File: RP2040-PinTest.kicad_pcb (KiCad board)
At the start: 2 copper layers, 57.2 x 53.3 mm, 3 parts

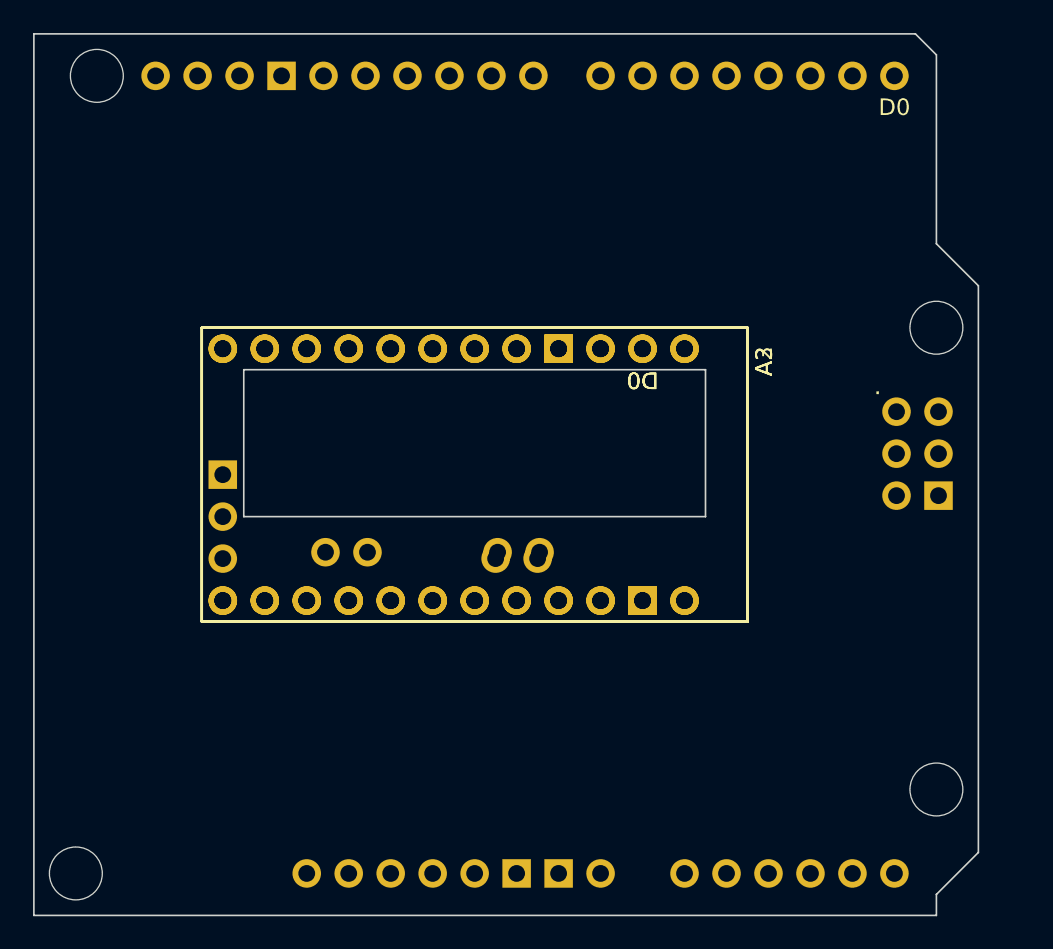
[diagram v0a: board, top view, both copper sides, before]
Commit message: Added more pins
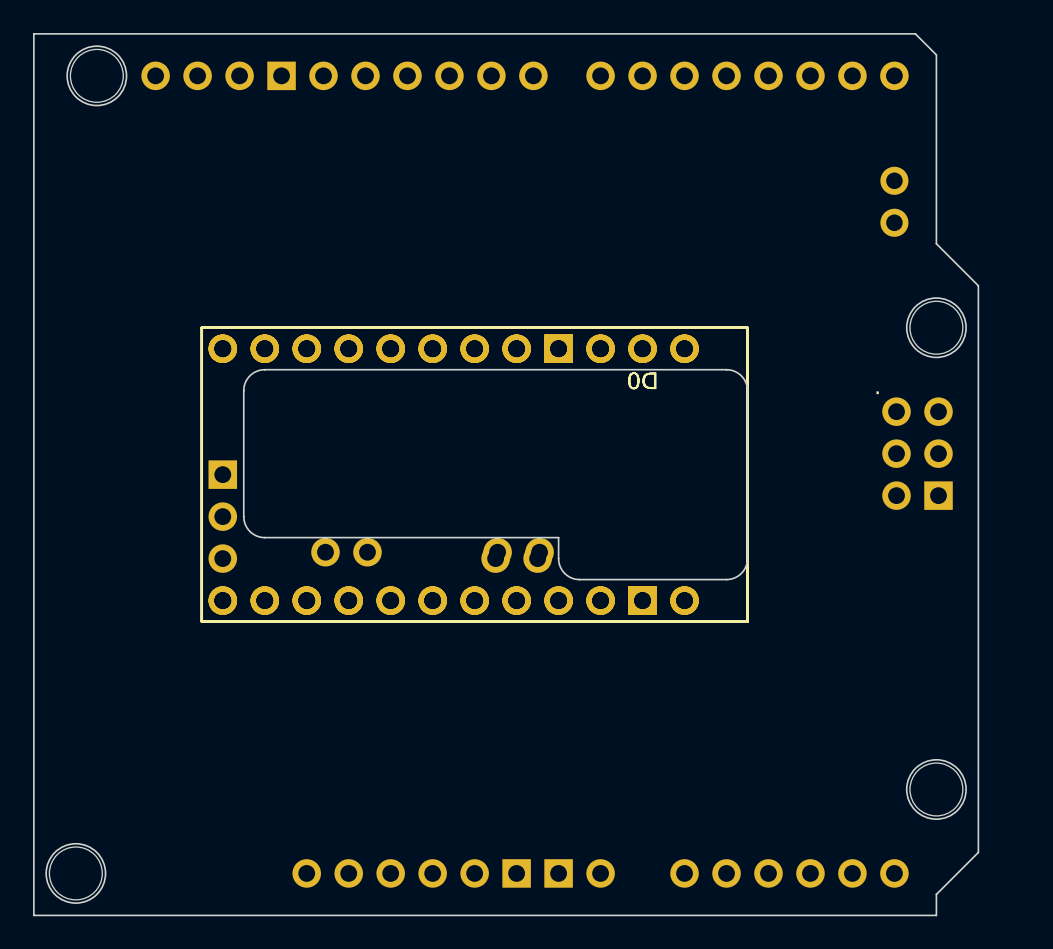
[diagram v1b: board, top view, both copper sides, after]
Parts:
- added J1: Conn_01x02_Socket, Connector_PinSocket_2.54mm:PinSocket_1x02_P2.54mm_Vertical, B.Cu at (182.9, 81.3)
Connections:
- A2 pad GND1: unconnected-(A2-GND-PadGND1) -> GND
- A2 pad GND2: unconnected-(A2-GND-PadGND2) -> GND
- A2 pad GND3: unconnected-(A2-GND-PadGND3) -> GND
- A3 pad GND1: unconnected-(A3-GND-PadGND1) -> GND
- A3 pad GND2: unconnected-(A3-GND-PadGND2) -> GND
- A4 pad GND1: unconnected-(A4-GND-PadGND1) -> GND
- A4 pad GND2: unconnected-(A4-GND-PadGND2) -> GND
- A4 pad GND3: unconnected-(A4-GND-PadGND3) -> GND
- A4 pad GND4: unconnected-(A4-SPI_GND-PadGND4) -> GND
- A4 pad MISO: unconnected-(A4-SPI_MISO-PadMISO) -> MISO
- A4 pad MOSI: unconnected-(A4-SPI_MOSI-PadMOSI) -> MOSI
- A4 pad SCK: unconnected-(A4-SPI_SCK-PadSCK) -> CSK
- A4 pad SCL: unconnected-(A4-PadSCL) -> SCL
- A4 pad SDA: unconnected-(A4-PadSDA) -> SDA
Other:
- outline, holes or cut-outs redrawn

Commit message: Added LEDs and basic routing
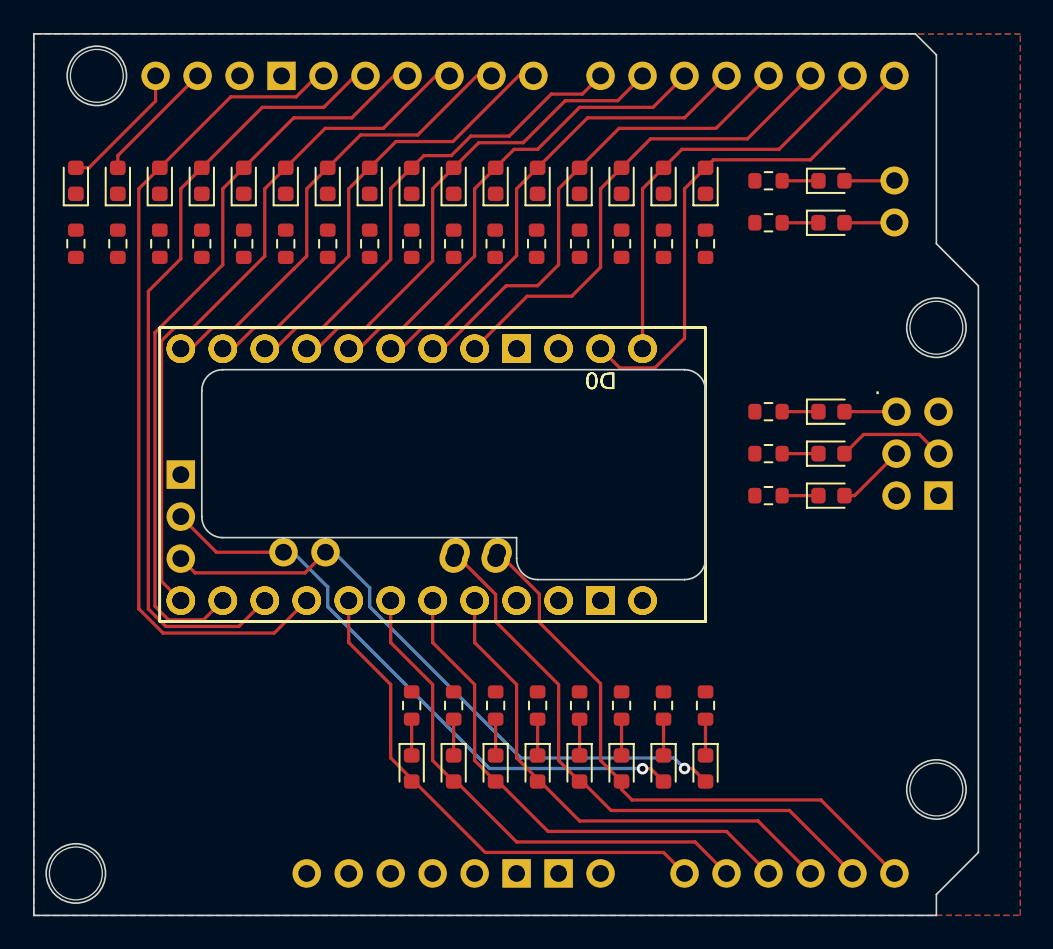
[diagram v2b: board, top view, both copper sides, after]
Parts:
- added D1: YELLOW, LED_SMD:LED_0603_1608Metric, F.Cu at (171.4, 81.3)
- added D10: YELLOW, LED_SMD:LED_0603_1608Metric, F.Cu at (148.6, 81.3)
- added D11: YELLOW, LED_SMD:LED_0603_1608Metric, F.Cu at (146.1, 81.3)
- added D12: YELLOW, LED_SMD:LED_0603_1608Metric, F.Cu at (143.5, 81.3)
- added D13: YELLOW, LED_SMD:LED_0603_1608Metric, F.Cu at (141.0, 81.3)
- added D14: YELLOW, LED_SMD:LED_0603_1608Metric, F.Cu at (138.4, 81.3)
- added D15: YELLOW, LED_SMD:LED_0603_1608Metric, F.Cu at (133.3, 81.3)
- added D16: YELLOW, LED_SMD:LED_0603_1608Metric, F.Cu at (135.9, 81.3)
- added D17: YELLOW, LED_SMD:LED_0603_1608Metric, F.Cu at (179.1, 95.2)
- added D18: YELLOW, LED_SMD:LED_0603_1608Metric, F.Cu at (179.1, 97.8)
- added D19: YELLOW, LED_SMD:LED_0603_1608Metric, F.Cu at (179.1, 100.3)
- added D2: YELLOW, LED_SMD:LED_0603_1608Metric, F.Cu at (168.9, 81.3)
- added D20: YELLOW, LED_SMD:LED_0603_1608Metric, F.Cu at (153.7, 116.8)
- added D21: YELLOW, LED_SMD:LED_0603_1608Metric, F.Cu at (156.2, 116.8)
- added D22: YELLOW, LED_SMD:LED_0603_1608Metric, F.Cu at (158.8, 116.8)
- added D23: YELLOW, LED_SMD:LED_0603_1608Metric, F.Cu at (161.3, 116.8)
- added D24: YELLOW, LED_SMD:LED_0603_1608Metric, F.Cu at (163.8, 116.8)
- added D25: YELLOW, LED_SMD:LED_0603_1608Metric, F.Cu at (166.4, 116.8)
- added D26: YELLOW, LED_SMD:LED_0603_1608Metric, F.Cu at (168.9, 116.8)
- added D27: YELLOW, LED_SMD:LED_0603_1608Metric, F.Cu at (171.4, 116.8)
- added D28: YELLOW, LED_SMD:LED_0603_1608Metric, F.Cu at (179.1, 83.8)
- added D29: YELLOW, LED_SMD:LED_0603_1608Metric, F.Cu at (179.1, 81.3)
- added D3: YELLOW, LED_SMD:LED_0603_1608Metric, F.Cu at (166.4, 81.3)
- added D4: YELLOW, LED_SMD:LED_0603_1608Metric, F.Cu at (163.8, 81.3)
- added D5: YELLOW, LED_SMD:LED_0603_1608Metric, F.Cu at (161.3, 81.3)
- added D6: YELLOW, LED_SMD:LED_0603_1608Metric, F.Cu at (158.8, 81.3)
- added D7: YELLOW, LED_SMD:LED_0603_1608Metric, F.Cu at (156.2, 81.3)
- added D8: YELLOW, LED_SMD:LED_0603_1608Metric, F.Cu at (153.7, 81.3)
- added D9: YELLOW, LED_SMD:LED_0603_1608Metric, F.Cu at (151.1, 81.3)
- added R1: 5k1, Resistor_SMD:R_0603_1608Metric, F.Cu at (171.4, 85.1)
- added R10: 5k1, Resistor_SMD:R_0603_1608Metric, F.Cu at (148.6, 85.1)
- added R11: 5k1, Resistor_SMD:R_0603_1608Metric, F.Cu at (146.1, 85.1)
- added R12: 5k1, Resistor_SMD:R_0603_1608Metric, F.Cu at (143.5, 85.1)
- added R13: 5k1, Resistor_SMD:R_0603_1608Metric, F.Cu at (141.0, 85.1)
- added R14: 5k1, Resistor_SMD:R_0603_1608Metric, F.Cu at (138.4, 85.1)
- added R15: 5k1, Resistor_SMD:R_0603_1608Metric, F.Cu at (133.3, 85.1)
- added R16: 5k1, Resistor_SMD:R_0603_1608Metric, F.Cu at (135.9, 85.1)
- added R17: 5k1, Resistor_SMD:R_0603_1608Metric, F.Cu at (175.3, 95.2)
- added R18: 5k1, Resistor_SMD:R_0603_1608Metric, F.Cu at (175.3, 97.8)
- added R19: 5k1, Resistor_SMD:R_0603_1608Metric, F.Cu at (175.3, 100.3)
- added R2: 5k1, Resistor_SMD:R_0603_1608Metric, F.Cu at (168.9, 85.1)
- added R20: 5k1, Resistor_SMD:R_0603_1608Metric, F.Cu at (153.7, 113.0)
- added R21: 5k1, Resistor_SMD:R_0603_1608Metric, F.Cu at (156.2, 113.0)
- added R22: 5k1, Resistor_SMD:R_0603_1608Metric, F.Cu at (158.8, 113.0)
- added R23: 5k1, Resistor_SMD:R_0603_1608Metric, F.Cu at (161.3, 113.0)
- added R24: 5k1, Resistor_SMD:R_0603_1608Metric, F.Cu at (163.8, 113.0)
- added R25: 5k1, Resistor_SMD:R_0603_1608Metric, F.Cu at (166.4, 113.0)
- added R26: 5k1, Resistor_SMD:R_0603_1608Metric, F.Cu at (168.9, 113.0)
- added R27: 5k1, Resistor_SMD:R_0603_1608Metric, F.Cu at (171.4, 113.0)
- added R28: 5k1, Resistor_SMD:R_0603_1608Metric, F.Cu at (175.3, 83.8)
- added R29: 5k1, Resistor_SMD:R_0603_1608Metric, F.Cu at (175.3, 81.3)
- added R3: 5k1, Resistor_SMD:R_0603_1608Metric, F.Cu at (166.4, 85.1)
- added R4: 5k1, Resistor_SMD:R_0603_1608Metric, F.Cu at (163.8, 85.1)
- added R5: 5k1, Resistor_SMD:R_0603_1608Metric, F.Cu at (161.2, 85.1)
- added R6: 5k1, Resistor_SMD:R_0603_1608Metric, F.Cu at (158.7, 85.1)
- added R7: 5k1, Resistor_SMD:R_0603_1608Metric, F.Cu at (156.2, 85.1)
- added R8: 5k1, Resistor_SMD:R_0603_1608Metric, F.Cu at (153.7, 85.1)
- added R9: 5k1, Resistor_SMD:R_0603_1608Metric, F.Cu at (151.1, 85.1)
- moved A2 2.54 mm to (154.9, 99.1)
- moved A3 2.54 mm to (154.9, 99.1)
- moved J1 2.52 mm to (182.9, 83.8), turned to 0 degrees
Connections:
- A4 pad SCK: CSK -> SCK
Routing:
- net D13: track 0.00 -> 51.0 mm
- net D12: track 0.00 -> 48.4 mm
- net D11: track 0.00 -> 45.9 mm
- net D10: track 0.00 -> 42.6 mm
- net A7: track 0.00 -> 39.0 mm, vias 0 -> 1
- net A6: track 0.00 -> 36.6 mm, vias 0 -> 1
- net A5: track 0.00 -> 36.1 mm
- net A4: track 0.00 -> 35.7 mm
- net A3: track 0.00 -> 31.3 mm
- net A2: track 0.00 -> 31.3 mm
- net A1: track 0.00 -> 31.3 mm
- net A0: track 0.00 -> 31.3 mm
- net D0: track 0.00 -> 30.9 mm
- net D2: track 0.00 -> 29.9 mm
- net D3: track 0.00 -> 29.9 mm
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- added copper zone on B.Cu, net GND
- added copper zone on F.Cu, net GND
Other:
- outline, holes or cut-outs redrawn

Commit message: Added few traces and vias
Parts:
- moved R5 0.06 mm to (161.3, 85.1)
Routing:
- net Net-(D9-K): track 0.00 -> 2.20 mm
- net Net-(D8-K): track 0.00 -> 2.20 mm
- net Net-(D7-K): track 0.00 -> 2.20 mm
- net Net-(D6-K): track 0.00 -> 2.20 mm
- net Net-(D5-K): track 0.00 -> 2.20 mm
- net Net-(D4-K): track 0.00 -> 2.20 mm
- net Net-(D3-K): track 0.00 -> 2.20 mm
- net Net-(D2-K): track 0.00 -> 2.20 mm
- net Net-(D16-K): track 0.00 -> 2.20 mm
- net Net-(D15-K): track 0.00 -> 2.20 mm
- net Net-(D14-K): track 0.00 -> 2.20 mm
- net Net-(D12-K): track 0.00 -> 2.20 mm
- net Net-(D11-K): track 0.00 -> 2.20 mm
- net Net-(D10-K): track 0.00 -> 2.20 mm
- net Net-(D1-K): track 0.00 -> 2.20 mm
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
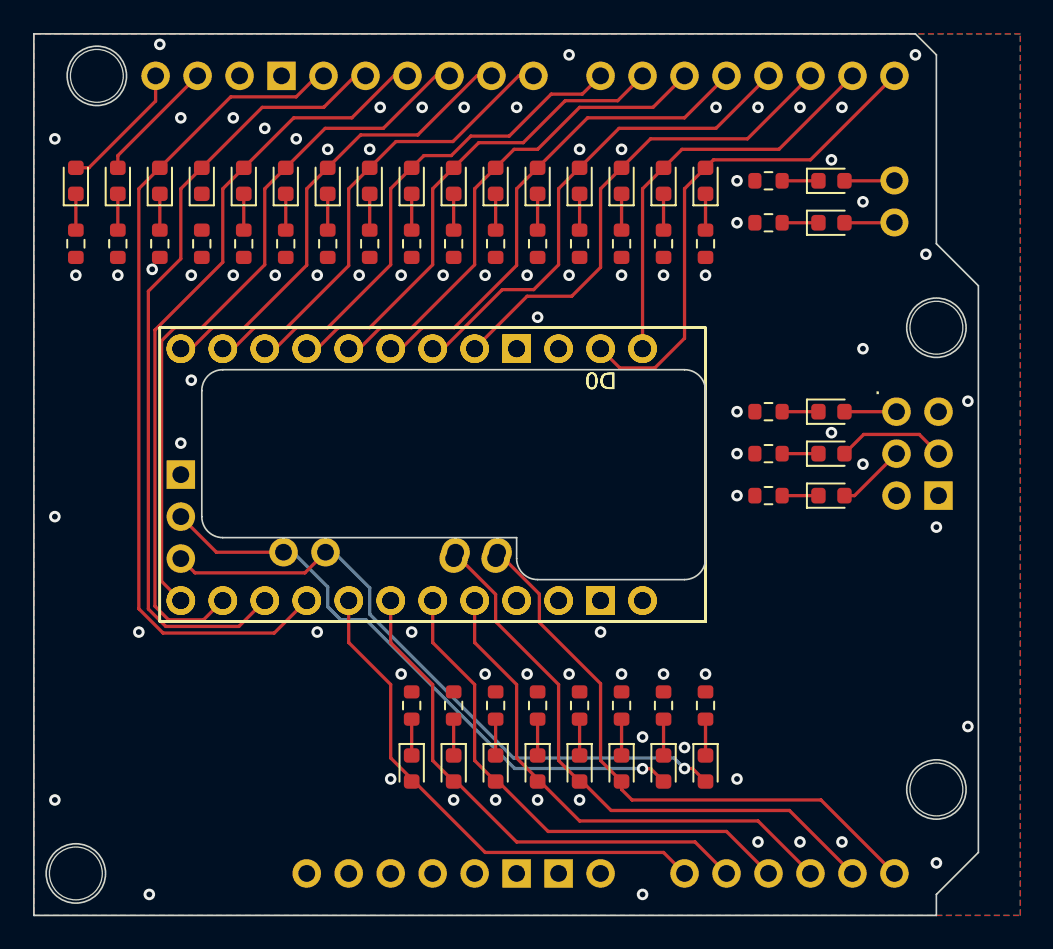
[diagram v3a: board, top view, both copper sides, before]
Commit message: Added few traces, vias and texts
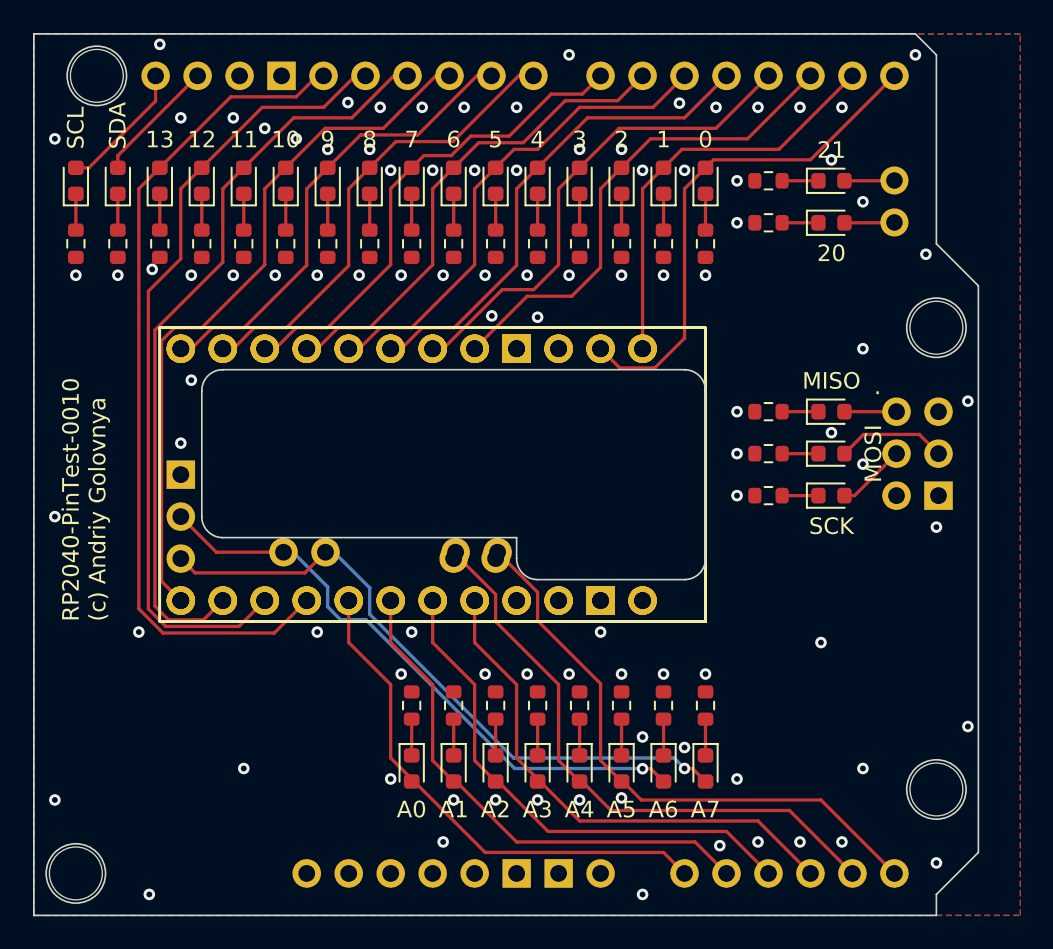
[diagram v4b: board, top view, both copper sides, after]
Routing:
- net Net-(D13-K): track 0.00 -> 2.20 mm
- net GND: vias 80 -> 95
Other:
- board text added: "${TITLE} ${COMPANY}"
- board text added: "0"
- board text added: "1"
- board text added: "10"
- board text added: "11"
- board text added: "12"
- board text added: "13"
- board text added: "2"
- board text added: "20"
- board text added: "21"
- board text added: "3"
- board text added: "4"
- board text added: "5"
- board text added: "6"
- board text added: "7"
- board text added: "8"
- board text added: "9"
- board text added: "A0"
- board text added: "A1"
- board text added: "A2"
- board text added: "A3"
- board text added: "A4"
- board text added: "A5"
- board text added: "A6"
- board text added: "A7"
- board text added: "MISO"
- board text added: "MOSI"
- board text added: "SCK"
- board text added: "SCL"
- board text added: "SDA"
